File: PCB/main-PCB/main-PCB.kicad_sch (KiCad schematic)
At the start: 27 parts, among them Q1 SSM6J214FE, Q2 Q_NMOS_GSD, U1 LIS2DU12TR, U2 STM32U031K4Ux

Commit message: Add heartbeat LED PWM pattern and low-power sleep/wake cycle
- Drive the heart LED via TIM2 CH4 PWM with a two-phase "lub-dub"
  ramp pattern, rest period scaled by accelerometer movement score
- Configure LIS2DU12 wake-up-on-motion (INT2) and enter STM32
  Shutdown mode after a period of no movement
- Set unused GPIOs to analog mode before shutdown to eliminate
  floating-pin leakage
- Bump reverse-polarity protection gate resistor (R1) from 100k to
  2M on the PCB, cutting its static draw from 30uA to ~1.5uA
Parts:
- removed C1, C4: 10uF, Capacitor_SMD:C_0402_1005Metric, symbol Device:C
- added C10, C11: 1uF, Capacitor_SMD:C_0603_1608Metric, symbol Device:C
- C9: footprint Capacitor_SMD:C_0402_1005Metric -> Capacitor_SMD:C_0603_1608Metric
- R1: value 100k -> 10M
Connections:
- net GND: now also C10.2, C11.2
- net VCC: now also C10.1, C11.1
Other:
- note added: "Select higher voltage rating caps to get slightly lower leakage current"
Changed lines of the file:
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@@
 		)
 	)
+	(text "Select higher voltage rating caps\nto get slightly lower leakage current"
+		(exclude_from_sim no)
+		(at 138.684 53.086 0)
+		(effects
+			(font
+				(size 1.27 1.27)
+			)
+		)
+	)
 	(text "3V in"
 		(exclude_from_sim no)
@@
 	)
 	(symbol
-		(lib_id "Device:C")
-		(at 130.81 67.31 0)
-		(mirror y)
-		(unit 1)
-		(body_style 1)
-		(exclude_from_sim no)
-		(in_bom yes)
-		(on_board yes)
-		(in_pos_files yes)
-		(dnp no)
-		(property "Reference" "C4"
-			(at 127 66.0399 0)
-			(show_name no)
-			(do_not_autoplace no)
-			(effects
-				(font
-					(size 1.27 1.27)
-				)
-				(justify left)
-			)
-		)
-		(property "Value" "10uF"
-			(at 127 68.5799 0)
-			(show_name no)
-			(do_not_autoplace no)
-			(effects
-				(font
-					(size 1.27 1.27)
-				)
-				(justify left)
-			)
-		)
-		(property "Footprint" "Capacitor_SMD:C_0402_1005Metric"
-			(at 129.8448 71.12 0)
-			(hide yes)
-			(show_name no)
-			(do_not_autoplace no)
-			(effects
-				(font
-					(size 1.27 1.27)
-				)
-			)
-		)
-		(property "Datasheet" ""
-			(at 130.81 67.31 0)
-			(hide yes)
-			(show_name no)
-			(do_not_autoplace no)
-			(effects
-				(font
-					(size 1.27 1.27)
-				)
-			)
-		)
-		(property "Description" "Unpolarized capacitor"
-			(at 130.81 67.31 0)
-			(hide yes)
-			(show_name no)
-			(do_not_autoplace no)
-			(effects
-				(font
-					(size 1.27 1.27)
-				)
-			)
-		)
-		(pin "2"
-		)
-		(pin "1"
-		)
-		(instances
-			(project "main-PCB"
-				(path "/05d84283-74ff-469f-a29b-6104f656f1bf"
-					(reference "C4")
-					(unit 1)
-				)
-			)
-		)
-	)
-	(symbol
 		(lib_id "power:GND")
 		(at 204.47 124.46 0)
@@
 			)
 		)
-		(property "Footprint" "Capacitor_SMD:C_0402_1005Metric"
+		(property "Footprint" "Capacitor_SMD:C_0603_1608Metric"
 			(at 183.8452 71.12 0)
 			(hide yes)
@@
 	)
 	(symbol
-		(lib_id "Device:C")
-		(at 39.37 138.43 0)
-		(mirror y)
-		(unit 1)
-		(body_style 1)
-		(exclude_from_sim no)
-		(in_bom yes)
-		(on_board yes)
-		(in_pos_files yes)
-		(dnp no)
-		(property "Reference" "C1"
-			(at 35.56 137.1599 0)
-			(show_name no)
-			(do_not_autoplace no)
-			(effects
-				(font
-					(size 1.27 1.27)
-				)
-				(justify left)
-			)
-		)
-		(property "Value" "10uF"
-			(at 35.56 139.6999 0)
-			(show_name no)
-			(do_not_autoplace no)
-			(effects
-				(font
-					(size 1.27 1.27)
-				)
-				(justify left)
-			)
-		)
-		(property "Footprint" "Capacitor_SMD:C_0402_1005Metric"
-			(at 38.4048 142.24 0)
-			(hide yes)
-			(show_name no)
-			(do_not_autoplace no)
-			(effects
-				(font
-					(size 1.27 1.27)
-				)
-			)
-		)
-		(property "Datasheet" ""
-			(at 39.37 138.43 0)
-			(hide yes)
-			(show_name no)
-			(do_not_autoplace no)
-			(effects
-				(font
-					(size 1.27 1.27)
-				)
-			)
-		)
-		(property "Description" "Unpolarized capacitor"
-			(at 39.37 138.43 0)
-			(hide yes)
-			(show_name no)
-			(do_not_autoplace no)
-			(effects
-				(font
-					(size 1.27 1.27)
-				)
-			)
-		)
-		(pin "2"
-		)
-		(pin "1"
-		)
-		(instances
-			(project "main-PCB"
-				(path "/05d84283-74ff-469f-a29b-6104f656f1bf"
-					(reference "C1")
-					(unit 1)
-				)
-			)
-		)
-	)
-	(symbol
 		(lib_id "power:GND")
 		(at 74.93 83.82 0)
@@
 			)
 		)
-		(property "Value" "100k"
+		(property "Value" "10M"
 			(at 73.66 62.2299 0)
 			(show_name no)
@@
 	(symbol
 		(lib_id "Device:C")
+		(at 130.81 67.31 0)
+		(mirror y)
+		(unit 1)
+		(body_style 1)
+		(exclude_from_sim no)
+		(in_bom yes)
+		(on_board yes)
+		(in_pos_files yes)
+		(dnp no)
+		(property "Reference" "C10"
+			(at 127 66.0399 0)
+			(show_name no)
+			(do_not_autoplace no)
+			(effects
+				(font
+					(size 1.27 1.27)
+				)
+				(justify left)
+			)
+		)
+		(property "Value" "1uF"
+			(at 127 68.5799 0)
+			(show_name no)
+			(do_not_autoplace no)
+			(effects
+				(font
+					(size 1.27 1.27)
+				)
+				(justify left)
+			)
+		)
+		(property "Footprint" "Capacitor_SMD:C_0603_1608Metric"
+			(at 129.8448 71.12 0)
+			(hide yes)
+			(show_name no)
+			(do_not_autoplace no)
+			(effects
+				(font
+					(size 1.27 1.27)
+				)
+			)
+		)
+		(property "Datasheet" ""
+			(at 130.81 67.31 0)
+			(hide yes)
+			(show_name no)
+			(do_not_autoplace no)
+			(effects
+				(font
+					(size 1.27 1.27)
+				)
+			)
+		)
+		(property "Description" "Unpolarized capacitor"
+			(at 130.81 67.31 0)
+			(hide yes)
+			(show_name no)
+			(do_not_autoplace no)
+			(effects
+				(font
+					(size 1.27 1.27)
+				)
+			)
+		)
+		(pin "2"
+		)
+		(pin "1"
+		)
+		(instances
+			(project "main-PCB"
+				(path "/05d84283-74ff-469f-a29b-6104f656f1bf"
+					(reference "C10")
+					(unit 1)
+				)
+			)
+		)
+	)
+	(symbol
+		(lib_id "Device:C")
 		(at 170.18 67.31 0)
 		(unit 1)
@@
 					(unit 1)
 				)
+			)
+		)
+	)
+	(symbol
+		(lib_id "Device:C")
+		(at 39.37 138.43 0)
+		(mirror y)
+		(unit 1)
+		(body_style 1)
+		(exclude_from_sim no)
+		(in_bom yes)
+		(on_board yes)
+		(in_pos_files yes)
+		(dnp no)
+		(property "Reference" "C11"
+			(at 35.56 137.1599 0)
+			(show_name no)
+			(do_not_autoplace no)
+			(effects
+				(font
+					(size 1.27 1.27)
+				)
+				(justify left)
+			)
+		)
+		(property "Value" "1uF"
+			(at 35.56 139.6999 0)
+			(show_name no)
+			(do_not_autoplace no)
+			(effects
+				(font
+					(size 1.27 1.27)
+				)
+				(justify left)
+			)
+		)
+		(property "Footprint" "Capacitor_SMD:C_0603_1608Metric"
+			(at 38.4048 142.24 0)
+			(hide yes)
+			(show_name no)
+			(do_not_autoplace no)
+			(effects
+				(font
+					(size 1.27 1.27)
+				)
+			)
+		)
+		(property "Datasheet" ""
+			(at 39.37 138.43 0)
+			(hide yes)
+			(show_name no)
+			(do_not_autoplace no)
+			(effects
+				(font
+					(size 1.27 1.27)
+				)
+			)
+		)
+		(property "Description" "Unpolarized capacitor"
+			(at 39.37 138.43 0)
+			(hide yes)
+			(show_name no)
+			(do_not_autoplace no)
+			(effects
+				(font
+					(size 1.27 1.27)
+				)
+			)
+		)
+		(pin "2"
+		)
+		(pin "1"
+		)
+		(instances
+			(project "main-PCB"
+				(path "/05d84283-74ff-469f-a29b-6104f656f1bf"
+					(reference "C11")
+					(unit 1)
+				)

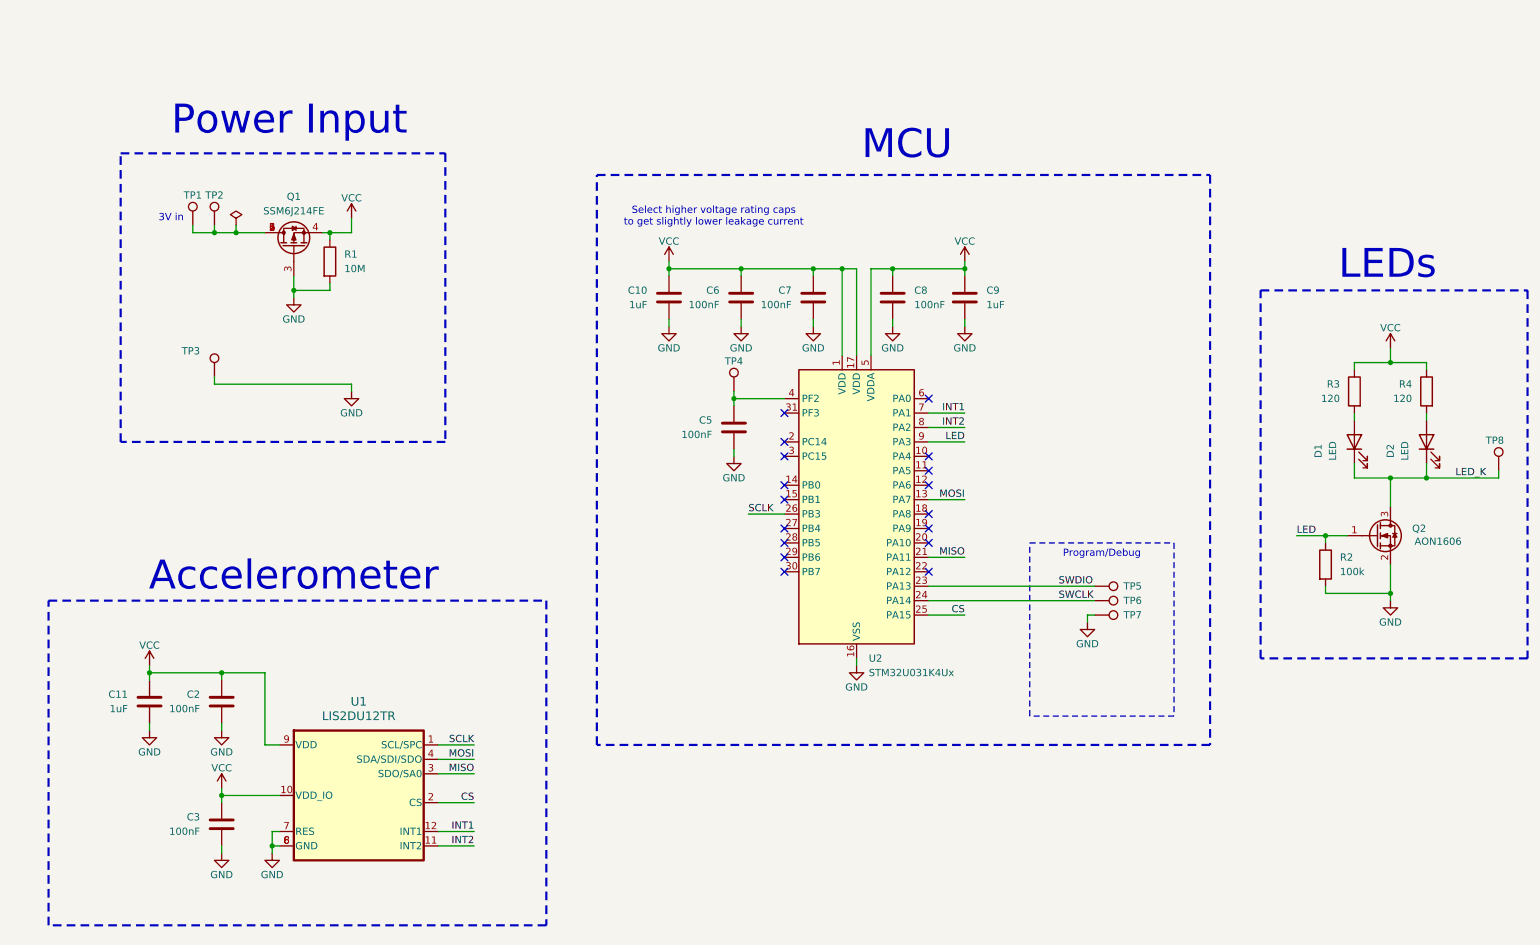
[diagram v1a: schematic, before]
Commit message: -In progress porting code to LIS2DW12.
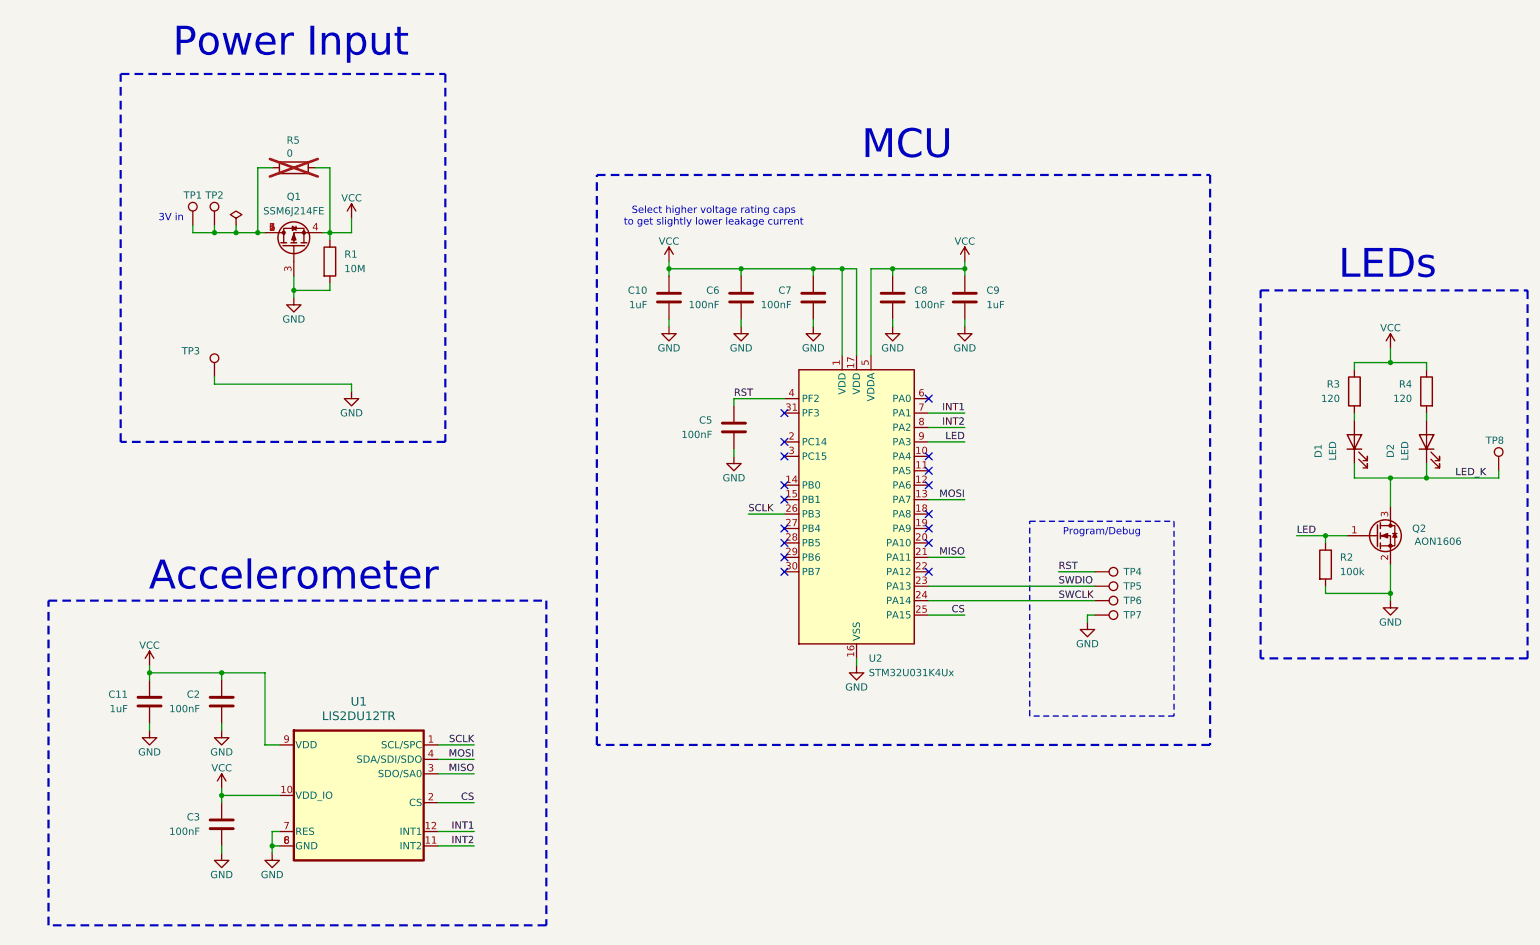
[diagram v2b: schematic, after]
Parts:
- added R5: 0, Resistor_SMD:R_0402_1005Metric, symbol Device:R
- TP4: footprint EN_Designs-Footprints:TestPoint_Pad_D0.5mm -> TestPoint:TestPoint_Pad_D1.0mm
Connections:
- net VCC: now also R5.1
- net RST: now reaches C5.1, TP4.1, U2.4 (PF2)
- net at Q1.1 (D), Q1.2 (D), Q1.5 (D)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: now also R5.2
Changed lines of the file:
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@@
 	)
 	(rectangle
-		(start 34.29 41.91)
+		(start 34.29 27.94)
 		(end 91.44 92.71)
 		(stroke
@@
 	(text "Power Input"
 		(exclude_from_sim no)
-		(at 64.008 39.116 0)
+		(at 64.262 25.4 0)
 		(effects
 			(font
@@
 	(text_box "Program/Debug"
 		(exclude_from_sim no)
-		(at 194.31 110.49 0)
-		(size 25.4 30.48)
+		(at 194.31 106.68 0)
+		(size 25.4 34.29)
 		(margins 0.9525 0.9525 0.9525 0.9525)
 		(stroke
@@
 	)
 	(junction
+		(at 58.42 55.88)
+		(diameter 0)
+		(color 0 0 0 0)
+	)
+	(junction
 		(at 264.16 99.06)
 		(diameter 0)
@@
 		(color 0 0 0 0)
 	)
-	(junction
-		(at 142.24 85.09)
-		(diameter 0)
-		(color 0 0 0 0)
-	)
 	(no_connect
 		(at 151.13 110.49)
@@
 	(wire
 		(pts
+			(xy 58.42 55.88) (xy 54.61 55.88)
+		)
+		(stroke
+			(width 0)
+			(type default)
+		)
+	)
+	(wire
+		(pts
 			(xy 52.07 156.21) (xy 52.07 154.94)
 		)
@@
 	(wire
 		(pts
-			(xy 170.18 71.12) (xy 170.18 72.39)
+			(xy 58.42 44.45) (xy 58.42 55.88)
 		)
 		(stroke
@@
 	(wire
 		(pts
-			(xy 163.83 62.23) (xy 161.29 62.23)
+			(xy 170.18 71.12) (xy 170.18 72.39)
 		)
 		(stroke
@@
 	(wire
 		(pts
-			(xy 130.81 62.23) (xy 143.51 62.23)
+			(xy 163.83 62.23) (xy 161.29 62.23)
 		)
 		(stroke
@@
 	(wire
 		(pts
-			(xy 60.96 165.1) (xy 60.96 163.83)
+			(xy 130.81 62.23) (xy 143.51 62.23)
 		)
 		(stroke
@@
 	(wire
 		(pts
-			(xy 176.53 118.11) (xy 205.74 118.11)
+			(xy 60.96 165.1) (xy 60.96 163.83)
 		)
 		(stroke
@@
 	(wire
 		(pts
-			(xy 142.24 83.82) (xy 142.24 85.09)
+			(xy 176.53 118.11) (xy 205.74 118.11)
 		)
 		(stroke
@@
 	(wire
 		(pts
-			(xy 59.69 55.88) (xy 54.61 55.88)
+			(xy 71.12 44.45) (xy 71.12 55.88)
+		)
+		(stroke
+			(width 0)
+			(type default)
+		)
+	)
+	(wire
+		(pts
+			(xy 59.69 55.88) (xy 58.42 55.88)
 		)
 		(stroke
@@
 	(wire
 		(pts
+			(xy 68.58 44.45) (xy 71.12 44.45)
+		)
+		(stroke
+			(width 0)
+			(type default)
+		)
+	)
+	(wire
+		(pts
 			(xy 264.16 99.06) (xy 276.86 99.06)
 		)
@@
 	(wire
 		(pts
+			(xy 60.96 44.45) (xy 58.42 44.45)
+		)
+		(stroke
+			(width 0)
+			(type default)
+		)
+	)
+	(wire
+		(pts
 			(xy 52.07 142.24) (xy 52.07 143.51)
 		)
@@
 	(wire
 		(pts
+			(xy 199.39 115.57) (xy 205.74 115.57)
+		)
+		(stroke
+			(width 0)
+			(type default)
+		)
+	)
+	(wire
+		(pts
 			(xy 204.47 123.19) (xy 204.47 124.46)
 		)
@@
 		)
 	)
+	(label "RST"
+		(at 199.39 115.57 0)
+		(effects
+			(font
+				(size 1.27 1.27)
+			)
+			(justify left bottom)
+		)
+	)
 	(label "MISO"
 		(at 182.88 113.03 180)
@@
 		)
 	)
+	(label "RST"
+		(at 142.24 85.09 0)
+		(effects
+			(font
+				(size 1.27 1.27)
+			)
+			(justify left bottom)
+		)
+	)
 	(label "MOSI"
 		(at 96.52 148.59 180)
@@
 	)
 	(symbol
+		(lib_id "Device:R")
+		(at 64.77 44.45 270)
+		(mirror x)
+		(unit 1)
+		(body_style 1)
+		(exclude_from_sim no)
+		(in_bom yes)
+		(on_board yes)
+		(in_pos_files yes)
+		(dnp yes)
+		(property "Reference" "R5"
+			(at 63.5 39.624 90)
+			(show_name no)
+			(do_not_autoplace no)
+			(effects
+				(font
+					(size 1.27 1.27)
+				)
+				(justify left)
+			)
+		)
+		(property "Value" "0"
+			(at 63.5001 41.91 90)
+			(show_name no)
+			(do_not_autoplace no)
+			(effects
+				(font
+					(size 1.27 1.27)
+				)
+				(justify left)
+			)
+		)
+		(property "Footprint" "Resistor_SMD:R_0402_1005Metric"
+			(at 64.77 46.228 90)
+			(hide yes)
+			(show_name no)
+			(do_not_autoplace no)
+			(effects
+				(font
+					(size 1.27 1.27)
+				)
+			)
+		)
+		(property "Datasheet" ""
+			(at 64.77 44.45 0)
+			(hide yes)
+			(show_name no)
+			(do_not_autoplace no)
+			(effects
+				(font
+					(size 1.27 1.27)
+				)
+			)
+		)
+		(property "Description" "Resistor"
+			(at 64.77 44.45 0)
+			(hide yes)
+			(show_name no)
+			(do_not_autoplace no)
+			(effects
+				(font
+					(size 1.27 1.27)
+				)
+			)
+		)
+		(pin "2"
+		)
+		(pin "1"
+		)
+		(instances
+			(project "main-PCB"
+				(path "/05d84283-74ff-469f-a29b-6104f656f1bf"
+					(reference "R5")
+					(unit 1)
+				)
+			)
+		)
+	)
+	(symbol
 		(lib_id "EN_Designs-Symbols:SSM6J214FE")
 		(at 64.77 55.88 90)
@@
 	)
 	(symbol
-		(lib_id "Connector:TestPoint")
-		(at 142.24 83.82 0)
-		(mirror y)
-		(unit 1)
-		(body_style 1)
-		(exclude_from_sim no)
-		(in_bom no)
-		(on_board yes)
-		(in_pos_files no)
-		(dnp no)
-		(property "Reference" "TP4"
-			(at 142.24 79.248 0)
-			(show_name no)
-			(do_not_autoplace no)
-			(effects
-				(font
-					(size 1.27 1.27)
-				)
-				(justify bottom)
-			)
-		)
-		(property "Value" "TestPoint"
-			(at 139.7 81.7879 0)
-			(hide yes)
-			(show_name no)
-			(do_not_autoplace no)
-			(effects
-				(font
-					(size 1.27 1.27)
-				)
-				(justify left)
-			)
-		)
-		(property "Footprint" "EN_Designs-Footprints:TestPoint_Pad_D0.5mm"
-			(at 137.16 83.82 0)
-			(hide yes)
-			(show_name no)
-			(do_not_autoplace no)
-			(effects
-				(font
-					(size 1.27 1.27)
-				)
-			)
-		)
-		(property "Datasheet" ""
-			(at 137.16 83.82 0)
-			(hide yes)
-			(show_name no)
-			(do_not_autoplace no)
-			(effects
-				(font
-					(size 1.27 1.27)
-				)
-			)
-		)
-		(property "Description" "test point"
-			(at 142.24 83.82 0)
-			(hide yes)
-			(show_name no)
-			(do_not_autoplace no)
-			(effects
-				(font
-					(size 1.27 1.27)
-				)
-			)
-		)
-		(pin "1"
-		)
-		(instances
-			(project "main-PCB"
-				(path "/05d84283-74ff-469f-a29b-6104f656f1bf"
-					(reference "TP4")
-					(unit 1)
-				)
-			)
-		)
-	)
-	(symbol
 		(lib_id "power:VCC")
 		(at 39.37 132.08 0)
@@
 					(unit 1)
 				)
+			)
+		)
+	)
+	(symbol
+		(lib_id "Connector:TestPoint")
+		(at 205.74 115.57 270)
+		(mirror x)
+		(unit 1)
+		(body_style 1)
+		(exclude_from_sim no)
+		(in_bom no)
+		(on_board yes)
+		(in_pos_files no)
+		(dnp no)
+		(property "Reference" "TP4"
+			(at 210.82 115.57 90)
+			(show_name no)
+			(do_not_autoplace no)
+			(effects
+				(font
+					(size 1.27 1.27)
+				)
+				(justify left)
+			)
+		)
+		(property "Value" "TestPoint"
+			(at 207.7721 113.03 0)
+			(hide yes)
+			(show_name no)
+			(do_not_autoplace no)
+			(effects
+				(font
+					(size 1.27 1.27)
+				)
+				(justify left)
+			)
+		)
+		(property "Footprint" "TestPoint:TestPoint_Pad_D1.0mm"
+			(at 205.74 110.49 0)
+			(hide yes)
+			(show_name no)
+			(do_not_autoplace no)
+			(effects
+				(font
+					(size 1.27 1.27)
+				)
+			)
+		)
+		(property "Datasheet" ""
+			(at 205.74 110.49 0)
+			(hide yes)
+			(show_name no)
+			(do_not_autoplace no)
+			(effects
+				(font
+					(size 1.27 1.27)
+				)
+			)
+		)
+		(property "Description" "test point"
+			(at 205.74 115.57 0)
+			(hide yes)
+			(show_name no)
+			(do_not_autoplace no)
+			(effects
+				(font
+					(size 1.27 1.27)
+				)
+			)
+		)
+		(pin "1"
+		)
+		(instances
+			(project "main-PCB"
+				(path "/05d84283-74ff-469f-a29b-6104f656f1bf"
+					(reference "TP4")
+					(unit 1)
+				)

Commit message: Changed optiisation, removed unused code, fixed bug of wrong flash size for KU4 chip
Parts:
- added TP10: TestPoint, TestPoint:TestPoint_Pad_D1.0mm, symbol Connector:TestPoint
- added TP15, TP4, TP5, TP6, TP7, TP8, TP9: TestPoint, EN_Designs-Footprints:TestPoint_Pad_D0.5mm, symbol Connector:TestPoint
- renumbered C11 to C1, C10 to C4, R5 to R1, R1 to R2, R2 to R3, R3 to R4, R4 to R5, TP4 to TP11, TP5 to TP12, TP6 to TP13, TP7 to TP14, TP8 to TP16
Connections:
- net CS: now also TP9.1
- net INT1: now also TP4.1
- net INT2: now also TP5.1
- net LED: now also TP15.1
- net MISO: now also TP8.1
- net MOSI: now also TP7.1
- net SCLK: now also TP6.1
- net TX: now reaches U2.19 (PA9)
- net TX: now also TP10.1
- no-connect marks 17 -> 16
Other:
- moved on the sheet: C1, C2, C3, U1
